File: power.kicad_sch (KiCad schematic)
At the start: 0 parts

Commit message: Finished power setup and cleared some mistakes
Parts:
- added C75, C77, C81: 1u, symbol Device:C
- added C79: 10u, symbol Device:C
- added C83: 0.1u, symbol Device:C
- added C87: 220n, symbol Device:C
- added C89: 100u, symbol Device:C
- added C91, C93: 22u, symbol Device:C
- added D43: TVS, symbol Diode:SMAJ28A
- added D45: LED, symbol Device:LED
- added D47: Zener, symbol Device:D_Zener
- added F1: Polyfuse, symbol Device:Polyfuse
- added L3: 1.5u, symbol Device:L
- added L5: 22u, symbol Device:L_Iron
- added Q1: PMOS, symbol Device:Q_PMOS_DSG
- added R185: 1K, symbol Device:R
- added R191: 100K, symbol Device:R
- added U33: LMR33620CQ5, Package_SO:Texas_HSOP-8-1EP_3.9x4.9mm_P1.27mm_ThermalVias, symbol Regulator_Switching:LMR33620ADDA
- added U35: TLV76733, Package_SON:WSON-6-1EP_2x2mm_P0.65mm_EP1x1.6mm_ThermalVias, symbol Regulator_Linear:TLV76733DRVx
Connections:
- new net: D45.1 (K), R185.1
- new net: C89.1, D45.2 (A), D47.1 (K), L5.1, Q1.2 (S)
- new net: C81.1, U33.6 (VCC)
- new net: D47.2 (A), Q1.3 (G), R191.1
- new net: C83.1, U33.7 (BOOT)
- new net: C83.2, L3.1, U33.8 (SW)
- new net: D43.1 (A1), F1.2, Q1.1 (D)
- new net +3V3: C77.1, U35.1 (OUT), U35.2 (SNS)
- new net +5V: C75.1, C91.1, C93.1, L3.2, U33.5 (FB), U35.4 (EN), U35.6 (IN)
- new net GND: C75.2, C77.2, C79.2, C81.2, C87.2, C89.2, C91.2, C93.2, D43.2 (A2), R185.2, R191.2, U33.1 (GND), U33.9 (GND), U35.3 (GND), U35.5 (GND), U35.7 (PAD)
- new net VCC: C79.1, C87.1, L5.2, U33.2 (VIN), U33.3 (EN)
- new net VDD: F1.1
- no-connect marks 0 -> 1

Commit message: Polished IO schematics
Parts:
- added U39: TPS2592xx, Package_SON:VSON-10-1EP_3x3mm_P0.5mm_EP1.65x2.4mm_ThermalVias, symbol Power_Management:TPS2592xx
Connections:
- new net: U39.3 (VIN), U39.4 (VIN), U39.5 (VIN)
- new net: U39.6 (OUT), U39.7 (OUT), U39.8 (OUT)
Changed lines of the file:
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@@
+    )
+  )
+  (symbol (lib_id "Power_Management:TPS2592xx") (at 120.65 31.75 0) (unit 1)
+    (in_bom yes) (on_board yes) (dnp no) (fields_autoplaced)
+    (property "Reference" "U39" (at 122.8441 21.59 0)
+      (effects (font (size 1.27 1.27)) (justify left))
+    )
+    (property "Value" "TPS2592xx" (at 122.8441 24.13 0)
+      (effects (font (size 1.27 1.27)) (justify left))
+    )
+    (property "Footprint" "Package_SON:VSON-10-1EP_3x3mm_P0.5mm_EP1.65x2.4mm_ThermalVias" (at 119.38 48.26 0)
+      (effects (font (size 1.27 1.27)) hide)
+    )
+    (property "Datasheet" "http://www.ti.com/lit/ds/symlink/tps25925.pdf" (at 110.49 21.59 0)
+      (effects (font (size 1.27 1.27)) hide)
+    )
+    (pin "9")
+    (pin "4")
+    (pin "3")
+    (pin "2")
+    (pin "10")
+    (pin "8")
+    (pin "6")
+    (pin "1")
+    (pin "7")
+    (pin "11")
+    (pin "5")
+    (instances
+      (project "cad-enc-dec"
+        (path "/894df1c3-1a5d-48b0-9966-84d5c2c2c705/1ddcf920-9630-4d5f-bf31-eeb8aa6bca02"
+          (reference "U39") (unit 1)
+        )
+        (path "/894df1c3-1a5d-48b0-9966-84d5c2c2c705/a384e571-8f3d-49bc-942a-9caee156865f"
+          (reference "U40") (unit 1)
+        )
+      )
     )
   )

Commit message: Set power routing for stm32
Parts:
- removed F1: Polyfuse, symbol Device:Polyfuse
- removed U39: TPS2592xx, Package_SON:VSON-10-1EP_3x3mm_P0.5mm_EP1.65x2.4mm_ThermalVias, symbol Power_Management:TPS2592xx
- added F3: Fuse, symbol Device:Fuse
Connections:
- net VDD: now also F3.1
- net at D43.1 (A1), Q1.1 (D): now also F3.2
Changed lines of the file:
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@@
+    )
+  )
+  (symbol (lib_id "Device:Fuse") (at 71.12 53.34 90) (unit 1)
+    (in_bom yes) (on_board yes) (dnp no) (fields_autoplaced)
+    (property "Reference" "F3" (at 71.12 48.26 90)
+      (effects (font (size 1.27 1.27)))
+    )
+    (property "Value" "Fuse" (at 71.12 50.8 90)
+      (effects (font (size 1.27 1.27)))
+    )
+    (property "Footprint" "" (at 71.12 55.118 90)
+      (effects (font (size 1.27 1.27)) hide)
+    )
+    (property "Datasheet" "~" (at 71.12 53.34 0)
+      (effects (font (size 1.27 1.27)) hide)
+    )
+    (pin "1")
+    (pin "2")
+    (instances
+      (project "cad-enc-dec"
+        (path "/894df1c3-1a5d-48b0-9966-84d5c2c2c705/1ddcf920-9630-4d5f-bf31-eeb8aa6bca02"
+          (reference "F3") (unit 1)
+        )
+        (path "/894df1c3-1a5d-48b0-9966-84d5c2c2c705/a384e571-8f3d-49bc-942a-9caee156865f"
+          (reference "F4") (unit 1)
+        )
+      )
     )
   )
@@
     )
   )
-  (symbol (lib_id "Device:Polyfuse") (at 71.12 53.34 90) (unit 1)
-    (in_bom yes) (on_board yes) (dnp no) (fields_autoplaced)
-    (property "Reference" "F1" (at 71.12 46.99 90)
-      (effects (font (size 1.27 1.27)))
-    )
-    (property "Value" "Polyfuse" (at 71.12 49.53 90)
-      (effects (font (size 1.27 1.27)))
-    )
-    (property "Footprint" "" (at 76.2 52.07 0)
-      (effects (font (size 1.27 1.27)) (justify left) hide)
-    )
-    (property "Datasheet" "~" (at 71.12 53.34 0)
-      (effects (font (size 1.27 1.27)) hide)
-    )
-    (pin "2")
-    (pin "1")
-    (instances
-      (project "cad-enc-dec"
-        (path "/894df1c3-1a5d-48b0-9966-84d5c2c2c705/1ddcf920-9630-4d5f-bf31-eeb8aa6bca02"
-          (reference "F1") (unit 1)
-        )
-        (path "/894df1c3-1a5d-48b0-9966-84d5c2c2c705/a384e571-8f3d-49bc-942a-9caee156865f"
-          (reference "F2") (unit 1)
-        )
-      )
-    )
-  )
   (symbol (lib_id "power:GND") (at 107.95 85.09 0) (unit 1)
     (in_bom yes) (on_board yes) (dnp no) (fields_autoplaced)
@@
         )
       )
-    )
-  )
-  (symbol (lib_id "Power_Management:TPS2592xx") (at 120.65 31.75 0) (unit 1)
-    (in_bom yes) (on_board yes) (dnp no) (fields_autoplaced)
-    (property "Reference" "U39" (at 122.8441 21.59 0)
-      (effects (font (size 1.27 1.27)) (justify left))
-    )
-    (property "Value" "TPS2592xx" (at 122.8441 24.13 0)
-      (effects (font (size 1.27 1.27)) (justify left))
-    )
-    (property "Footprint" "Package_SON:VSON-10-1EP_3x3mm_P0.5mm_EP1.65x2.4mm_ThermalVias" (at 119.38 48.26 0)
-      (effects (font (size 1.27 1.27)) hide)
-    )
-    (property "Datasheet" "http://www.ti.com/lit/ds/symlink/tps25925.pdf" (at 110.49 21.59 0)
-      (effects (font (size 1.27 1.27)) hide)
-    )
-    (pin "9")
-    (pin "4")
-    (pin "3")
-    (pin "2")
-    (pin "10")
-    (pin "8")
-    (pin "6")
-    (pin "1")
-    (pin "7")
-    (pin "11")
-    (pin "5")
-    (instances
-      (project "cad-enc-dec"
-        (path "/894df1c3-1a5d-48b0-9966-84d5c2c2c705/1ddcf920-9630-4d5f-bf31-eeb8aa6bca02"
-          (reference "U39") (unit 1)
-        )
-        (path "/894df1c3-1a5d-48b0-9966-84d5c2c2c705/a384e571-8f3d-49bc-942a-9caee156865f"
-          (reference "U40") (unit 1)
-        )
-      )

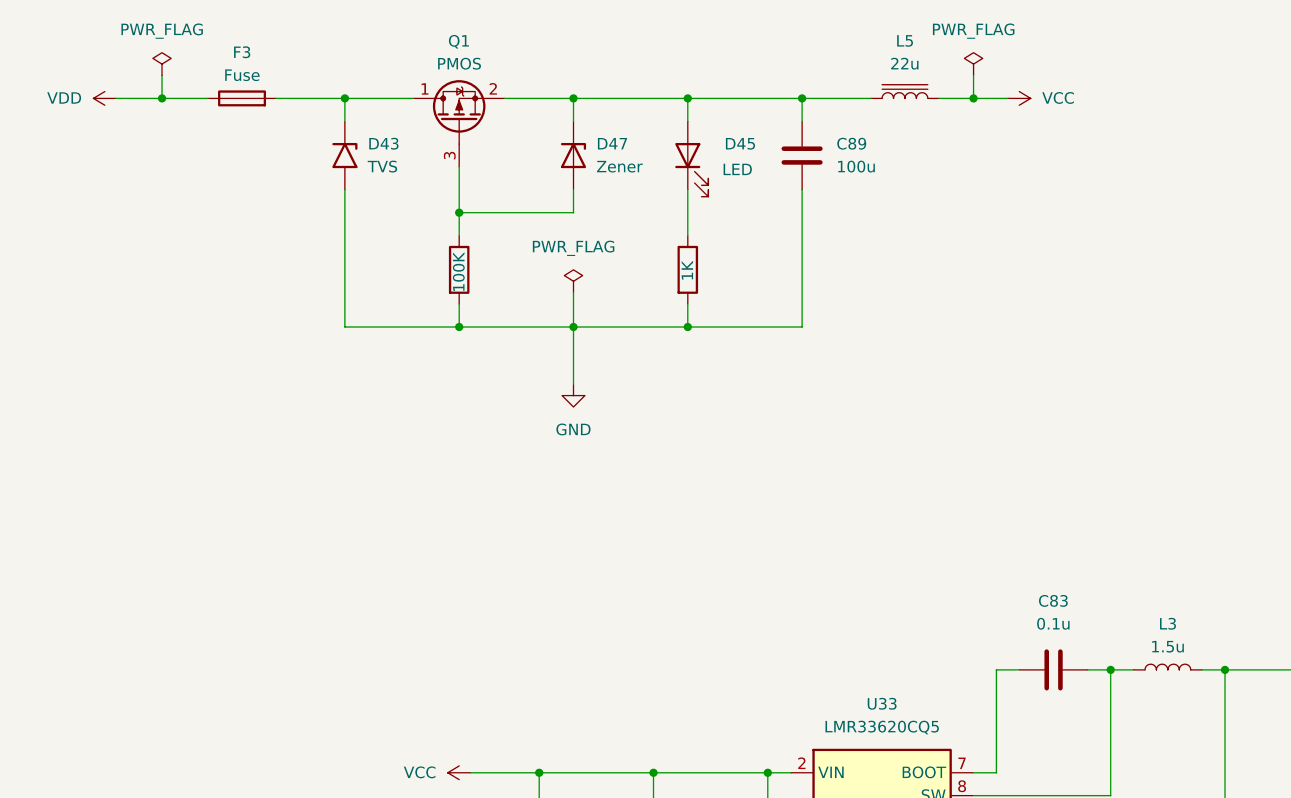
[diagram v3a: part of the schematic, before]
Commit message: Assigned proper footprints for all components
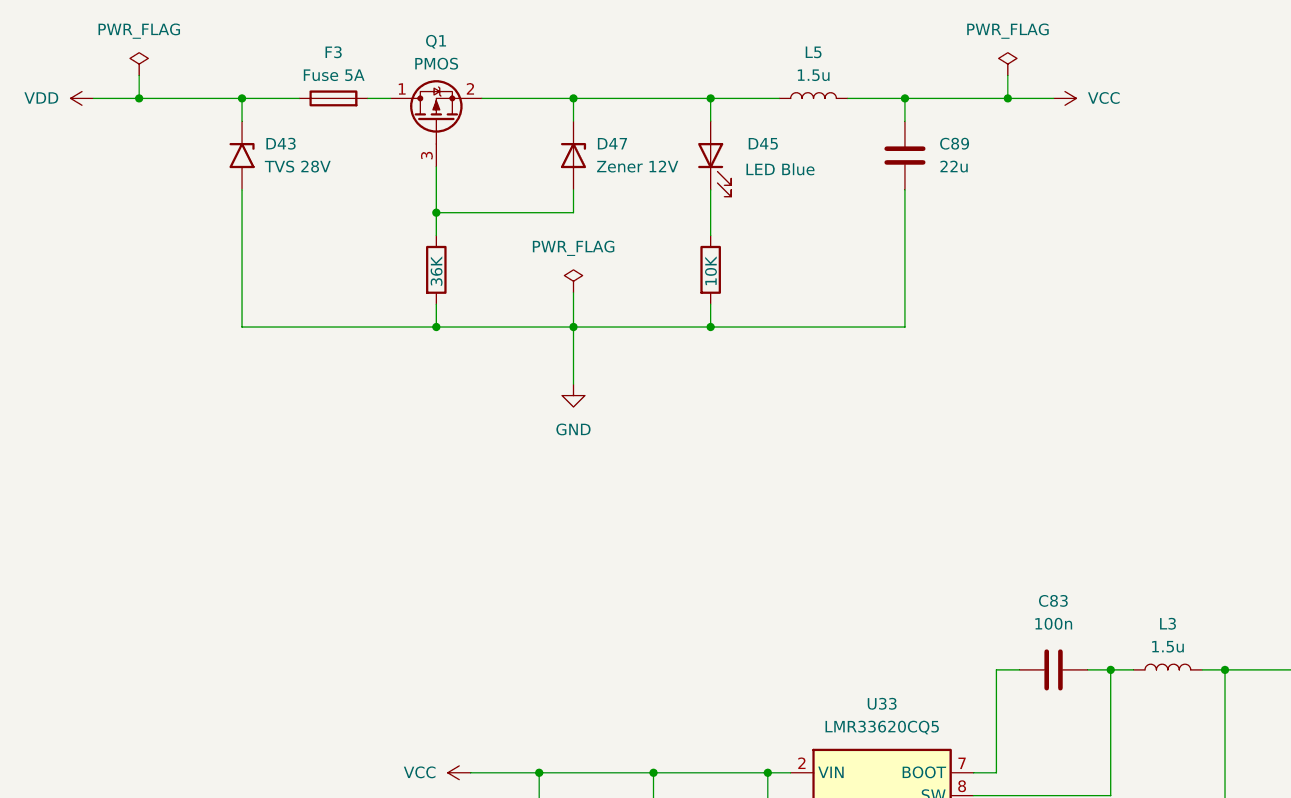
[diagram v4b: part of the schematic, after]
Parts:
- removed L5: 22u, symbol Device:L_Iron
- added L5: 1.5u, Inductor_SMD:L_Bourns-SRN4018, symbol Device:L
- C75, C77, C81: footprint (none) -> Capacitor_SMD:C_0805_2012Metric_Pad1.18x1.45mm_HandSolder
- C79, C91, C93: footprint (none) -> Capacitor_SMD:C_1206_3216Metric_Pad1.33x1.80mm_HandSolder
- C83: value 0.1u -> 100n; footprint (none) -> Capacitor_SMD:C_0603_1608Metric_Pad1.08x0.95mm_HandSolder
- C87: footprint (none) -> Capacitor_SMD:C_0603_1608Metric_Pad1.08x0.95mm_HandSolder
- C89: value 100u -> 22u; footprint (none) -> Capacitor_SMD:C_1206_3216Metric_Pad1.33x1.80mm_HandSolder
- D43: value TVS -> TVS 28V; footprint (none) -> Diode_SMD:D_SMA
- D45: value LED -> LED Blue; footprint (none) -> Diode_SMD:D_0603_1608Metric_Pad1.05x0.95mm_HandSolder
- D47: value Zener -> Zener 12V; footprint (none) -> Package_TO_SOT_SMD:SOT-23
- F3: value Fuse -> Fuse 5A; footprint (none) -> Fuse:Fuse_1812_4532Metric_Pad1.30x3.40mm_HandSolder
- L3: footprint (none) -> Inductor_SMD:L_Bourns-SRN4018
- Q1: footprint (none) -> Package_DFN_QFN:DFN-8-1EP_6x5mm_P1.27mm_EP4x4mm
- R185: value 1K -> 10K; footprint (none) -> Resistor_SMD:R_0603_1608Metric_Pad0.98x0.95mm_HandSolder
- R191: value 100K -> 36K; footprint (none) -> Resistor_SMD:R_0603_1608Metric_Pad0.98x0.95mm_HandSolder
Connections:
- net VCC: now also C89.1, L5.2
- net VDD: now also D43.1 (A1)
- net at D45.2 (A), D47.1 (K), Q1.2 (S): now also L5.1; no longer C89.1
- net at F3.2, Q1.1 (D): no longer D43.1 (A1)
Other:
- moved on the sheet: C89, D43, D45, F3, Q1

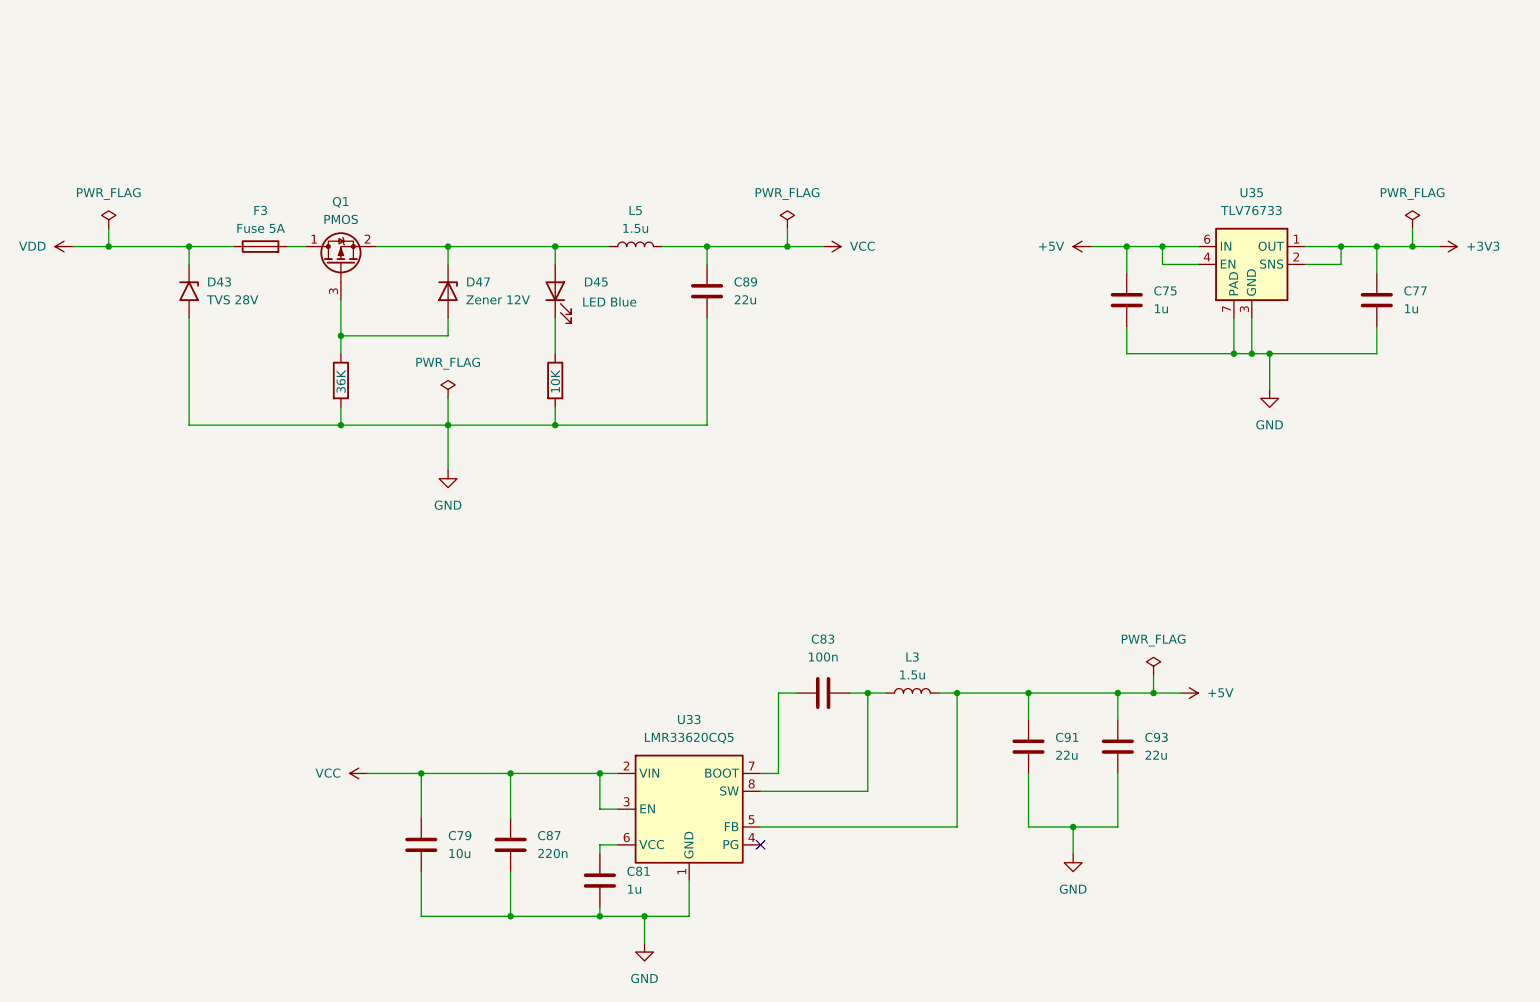
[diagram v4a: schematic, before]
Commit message: Updated boards hierarchy
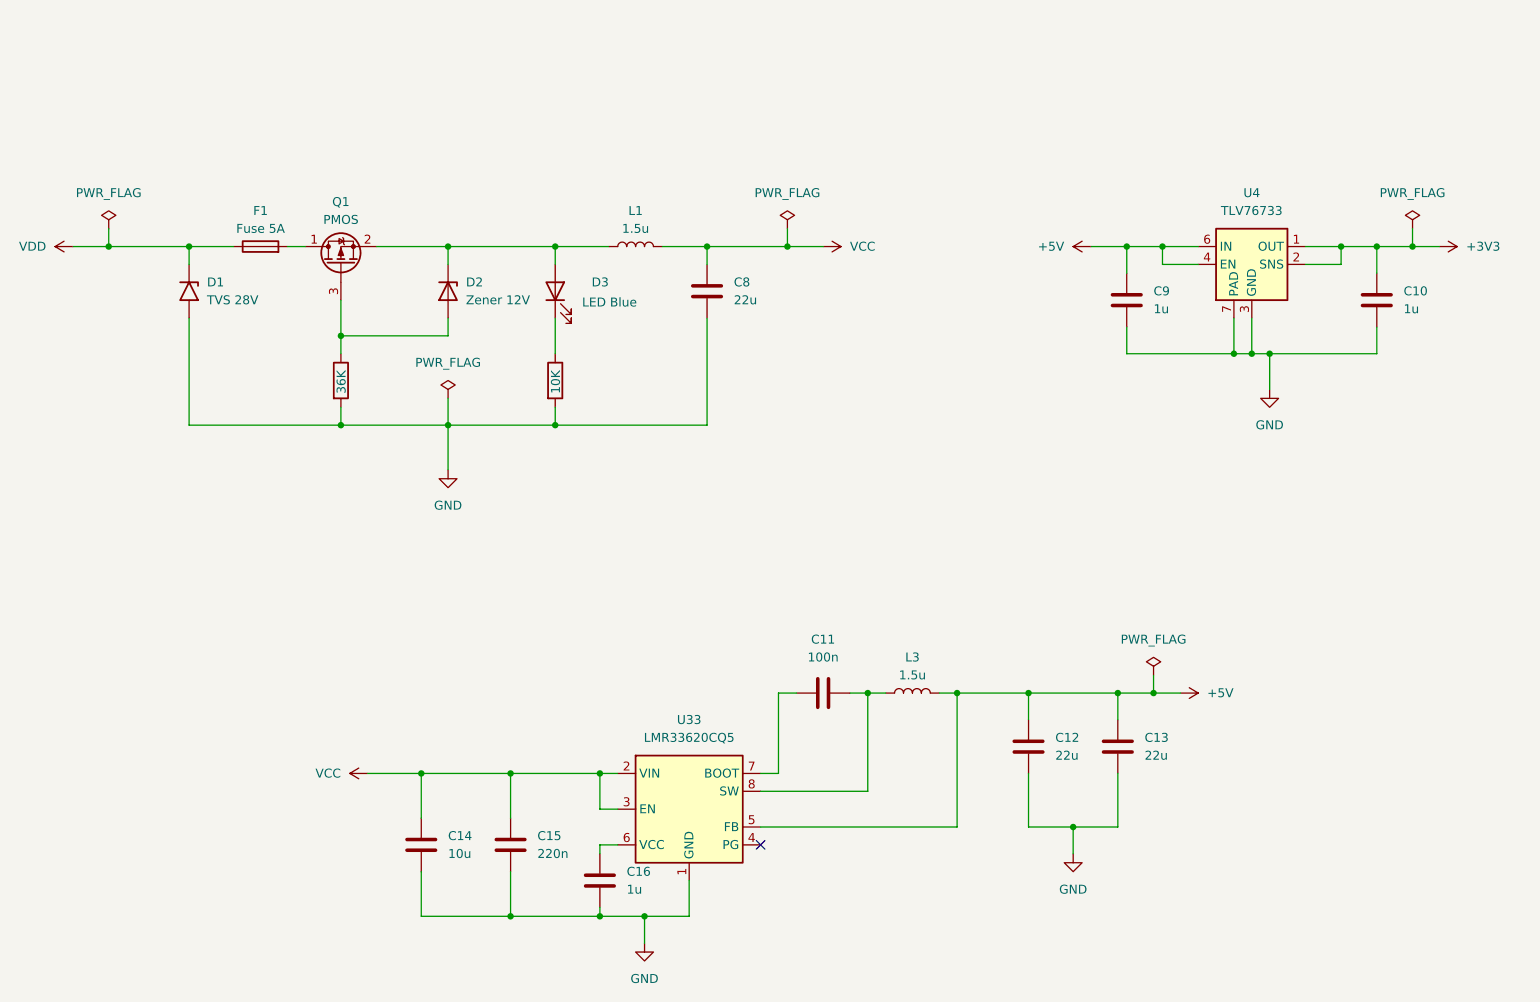
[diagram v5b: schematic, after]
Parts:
- renumbered C77 to C10, C83 to C11, C91 to C12, C93 to C13, C79 to C14, C87 to C15, C81 to C16, C89 to C8, C75 to C9, D43 to D1, D47 to D2, D45 to D3, F3 to F1, L5 to L1, R191 to R21, R185 to R22, U35 to U4

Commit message: Updated ethernet and power IO ports
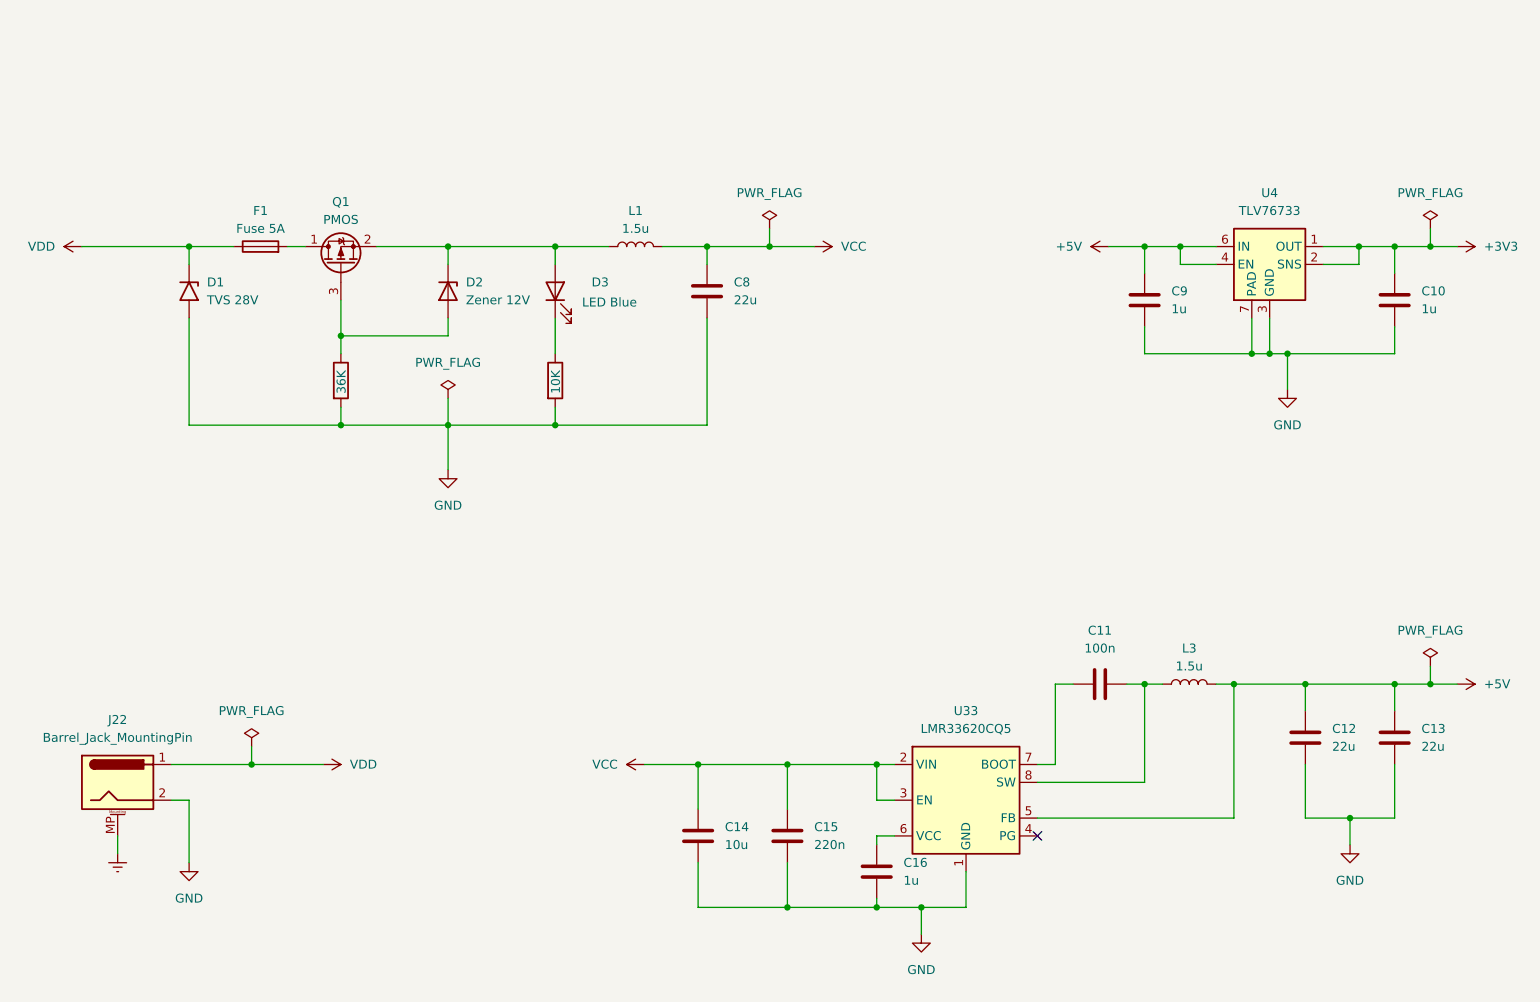
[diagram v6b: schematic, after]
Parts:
- added J22: Barrel_Jack_MountingPin, symbol Connector:Barrel_Jack_MountingPin
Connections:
- net GND: now also J22.2
- net VDD: now also J22.1
- new net Earth: J22.MP (MountPin)
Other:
- moved on the sheet: C10, C11, C12, C13, C14, C15, C16, C9, L3, U33, U4

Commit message: Finished annotation
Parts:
- renumbered C8 to C401, C9 to C402, C10 to C403, C11 to C404, C12 to C405, C13 to C406, C14 to C407, C15 to C408, C16 to C409, D1 to D401, D2 to D402, D3 to D403, F1 to F401, J22 to J401, L1 to L401, L3 to L402, Q1 to Q401, R21 to R401, R22 to R402, U4 to U401, U33 to U402

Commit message: Fixed ERC errors and warnings
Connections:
- net VCC renamed +24V
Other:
- moved on the sheet: C402, C403, J401, U401
